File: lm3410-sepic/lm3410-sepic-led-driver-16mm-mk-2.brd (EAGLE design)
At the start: 16 x 16 mm, 14 parts, among them IC2 ATTINY13

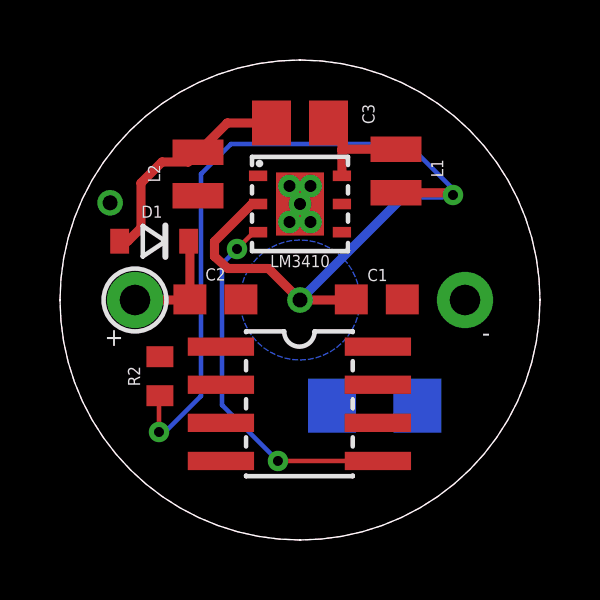
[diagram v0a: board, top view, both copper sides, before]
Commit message: 16mm version routed and ready for fabbing
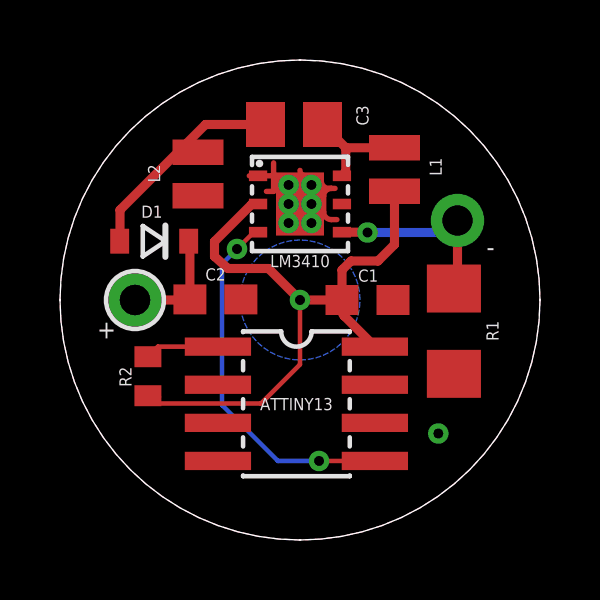
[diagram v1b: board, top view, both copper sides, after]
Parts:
- moved JBATT- 13.4 mm to (12.6, 3.55)
- moved R1 3.62 mm to (13.1, 6.96), flipped to the top, turned to 90 degrees
- moved - 2.66 mm to (13.2, 10.7)
- moved R2 0.40 mm to (2.93, 5.46)
- moved C1 0.31 mm to (10.2, 8.00)
- moved C3 0.21 mm to (7.80, 13.8)
- moved IC2 0.10 mm to (7.88, 4.54)
- moved L1 0.07 mm to (11.2, 12.3)
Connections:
- net N$3 renamed RST
- net V_BATT+ renamed VCC
- new net D1: IC2.6
- new net D2: IC2.7
- new net D3: IC2.2
- new net D4: IC2.3
- net GND: now also LM3410.7@6
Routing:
- net VCC: track 36.3 -> 22.4 mm, vias 2 -> 0
- net N$6: track 0.00 -> 6.34 mm, vias 0 -> 1
- net GND: track 0.00 -> 4.95 mm
- net RST: track 0.00 -> 2.47 mm
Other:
- board text added: "Septic SEPIC 16mm Rev 1.0 CC-BY-SA-4.0"
